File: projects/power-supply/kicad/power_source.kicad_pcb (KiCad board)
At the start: 4 copper layers, 176.2 x 104.8 mm, 64 parts, among them J1 Conn_01x03_out, J2 Conn_01x02_in, J3 Conn_Pos_meter_supply, J4 Conn_neg_meter_supply, J5 Fan2, J6 Fan1, J7 conn_pos_current_sense, J8 conn_neg_current_sense, Q1 SI4403DDY-T1-GE3, U1 AM2D-1505S-RZ, U2 AM2D-1505S-RZ, U3 LT3083ET#PBF, U4 LT3083ET#PBF, U5 LM2596S-ADJ_NOPB, U6 LT3091ET7#PBF, U7 LT3091ET7#PBF

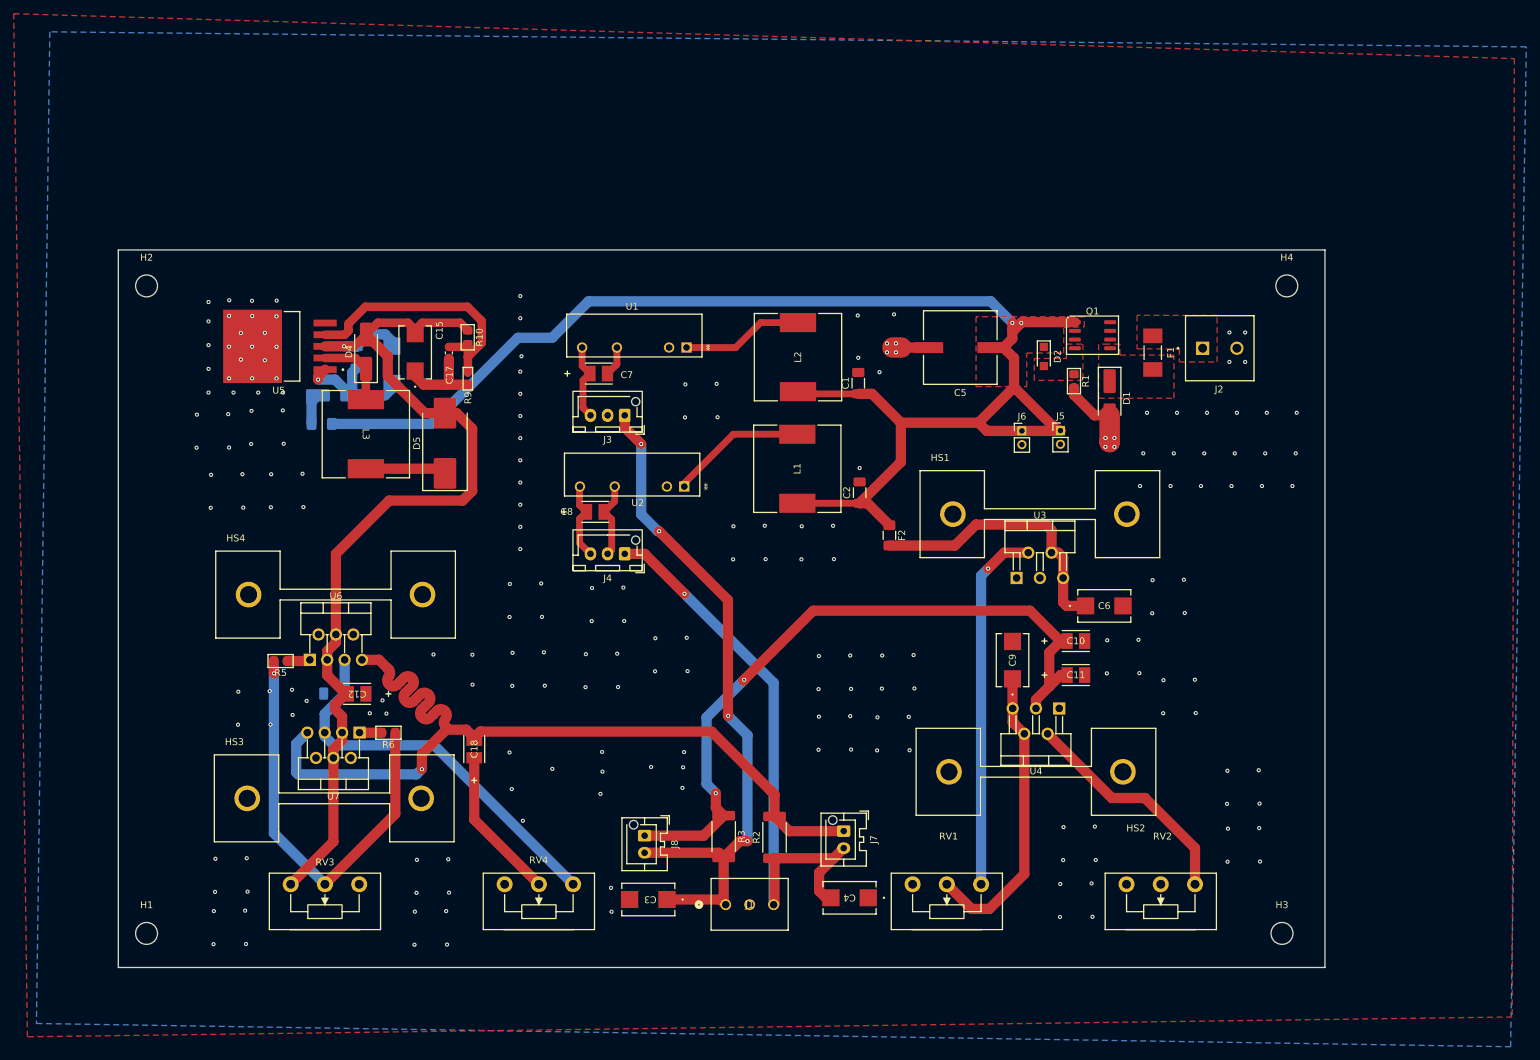
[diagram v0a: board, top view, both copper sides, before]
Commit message: updating kicad files for power supply
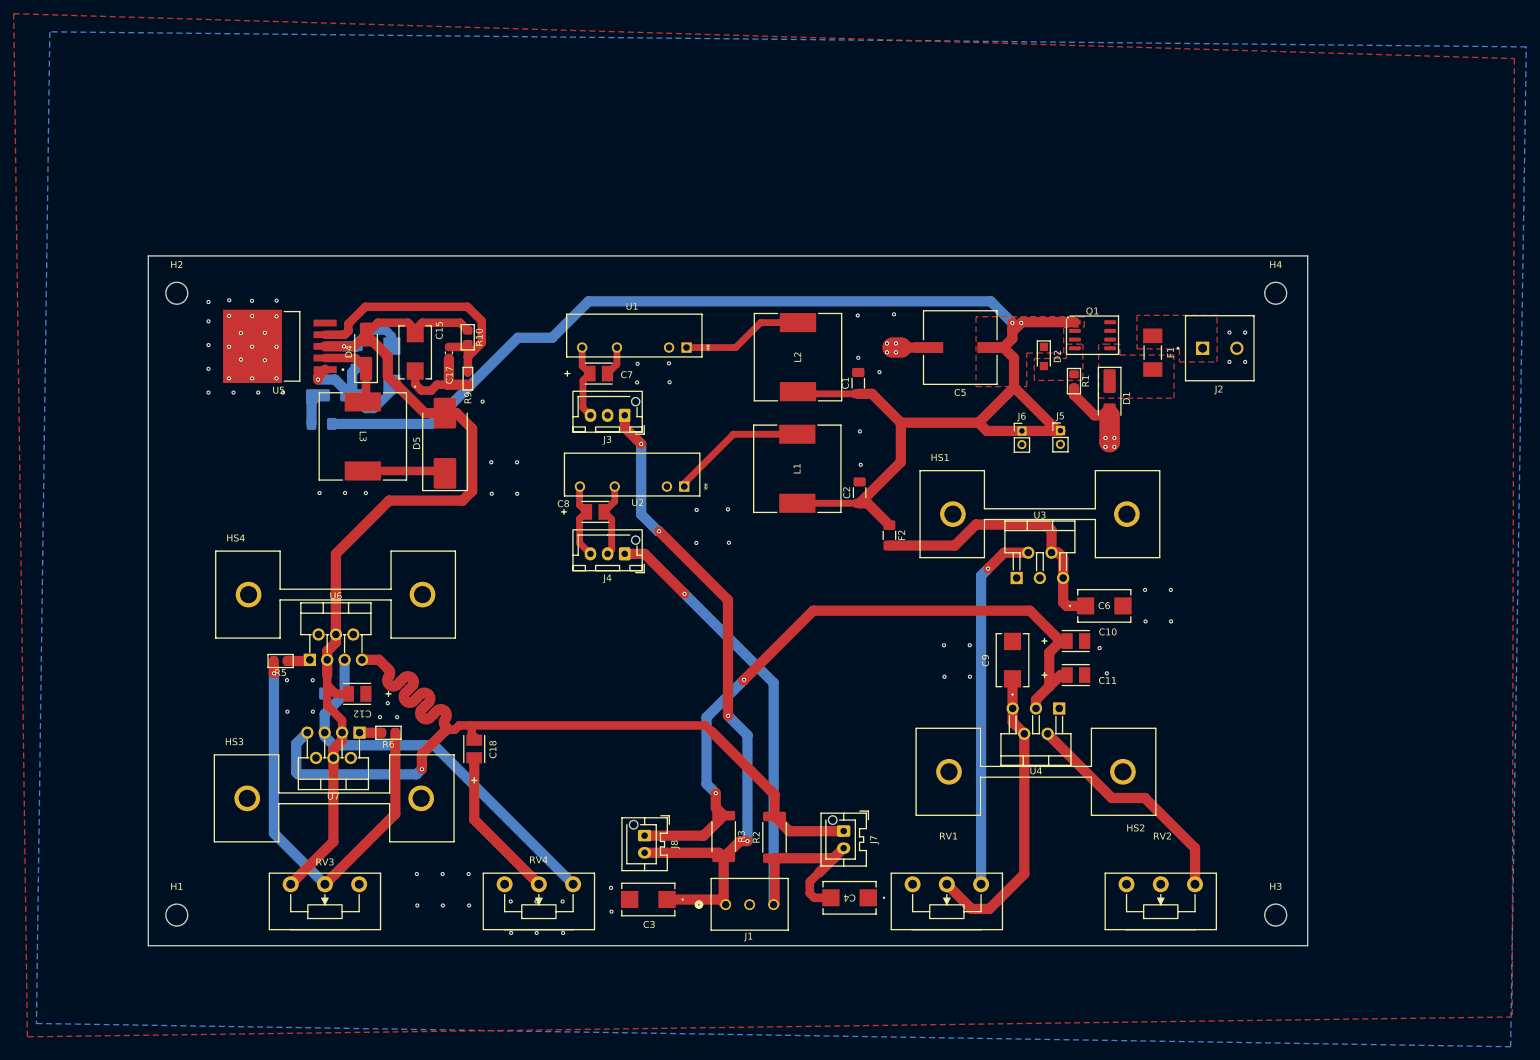
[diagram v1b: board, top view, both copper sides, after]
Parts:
- moved H1 5.16 mm to (41.1, 150.6)
- moved H2 4.54 mm to (41.1, 59.8)
- moved H3 2.83 mm to (201.6, 150.6)
- moved H4 1.94 mm to (201.6, 59.8)
- moved L3 0.55 mm to (68.3, 80.7)
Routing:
- net -11V: track 143.1 -> 146.6 mm
- net GND: track 68.0 -> 70.7 mm, vias 204 -> 89
- net Final_Neg_Out: track 87.3 -> 89.4 mm
- net Net-(D3-K): track 19.0 -> 20.9 mm
- net neg_reg_out_to_shunt: track 129.5 -> 131.2 mm
- net Net-(D4-K): track 11.1 -> 11.7 mm
- net (no net): vias 1 -> 0
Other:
- board size 176.2 x 104.8 mm -> 169.3 x 100.7 mm
